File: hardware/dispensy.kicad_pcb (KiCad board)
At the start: 2 copper layers, 125 x 100 mm, 87 parts, among them SW1 BOOTSEL, SW2 RESET, U1 DBT50G-7_62-4P, U10 RP2040, U11 SS54_C22452, U12 SS54_C22452, U13 CAN_IO, U14 TJA1042T_3_1J, U15 USB-C, U16 LM2576S-5_0_TR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

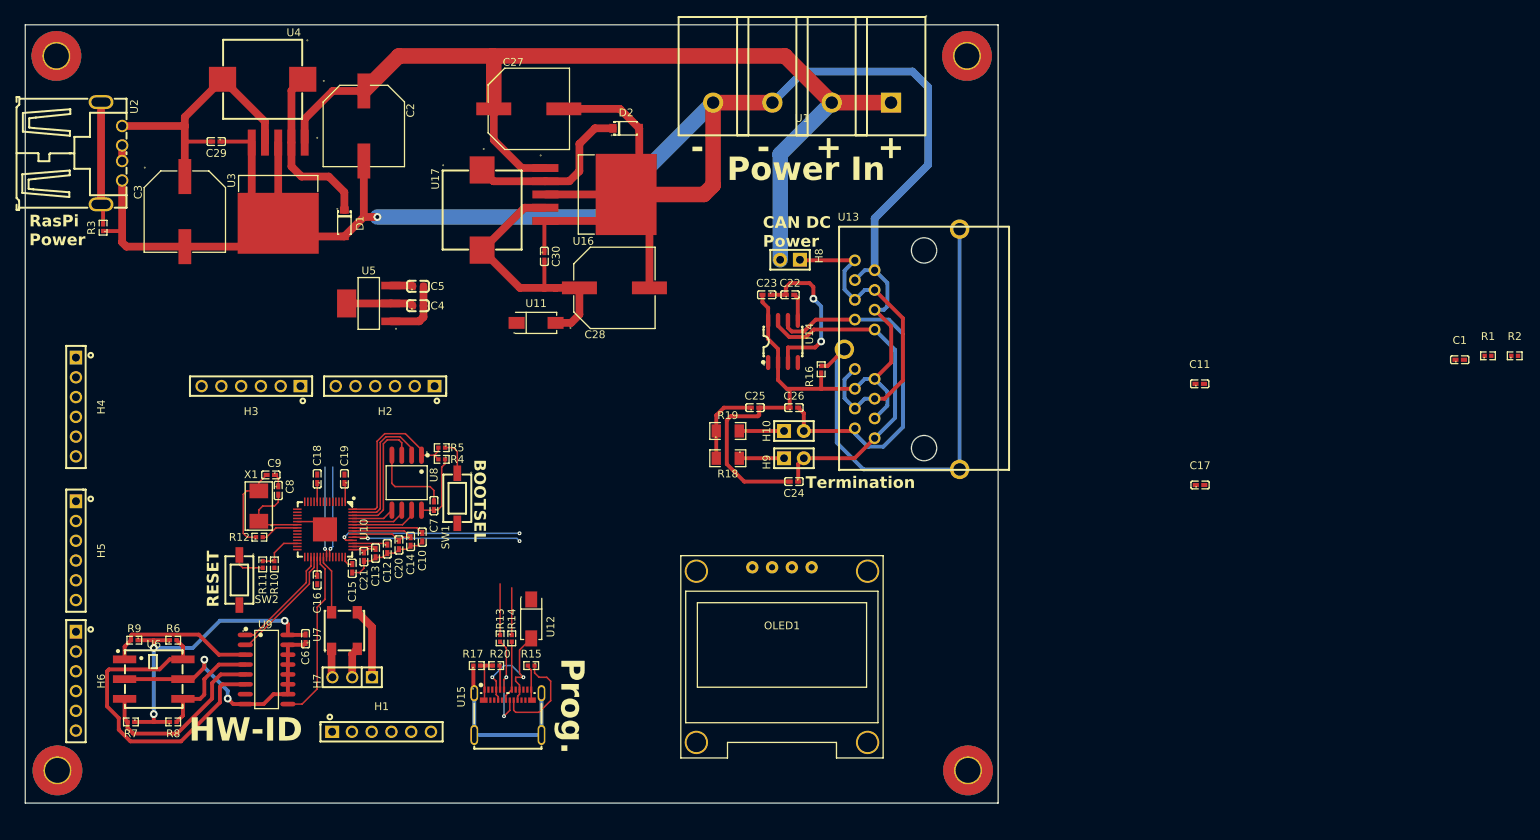
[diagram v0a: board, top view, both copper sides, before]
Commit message: more routing. all parts placed somewhere on board now.
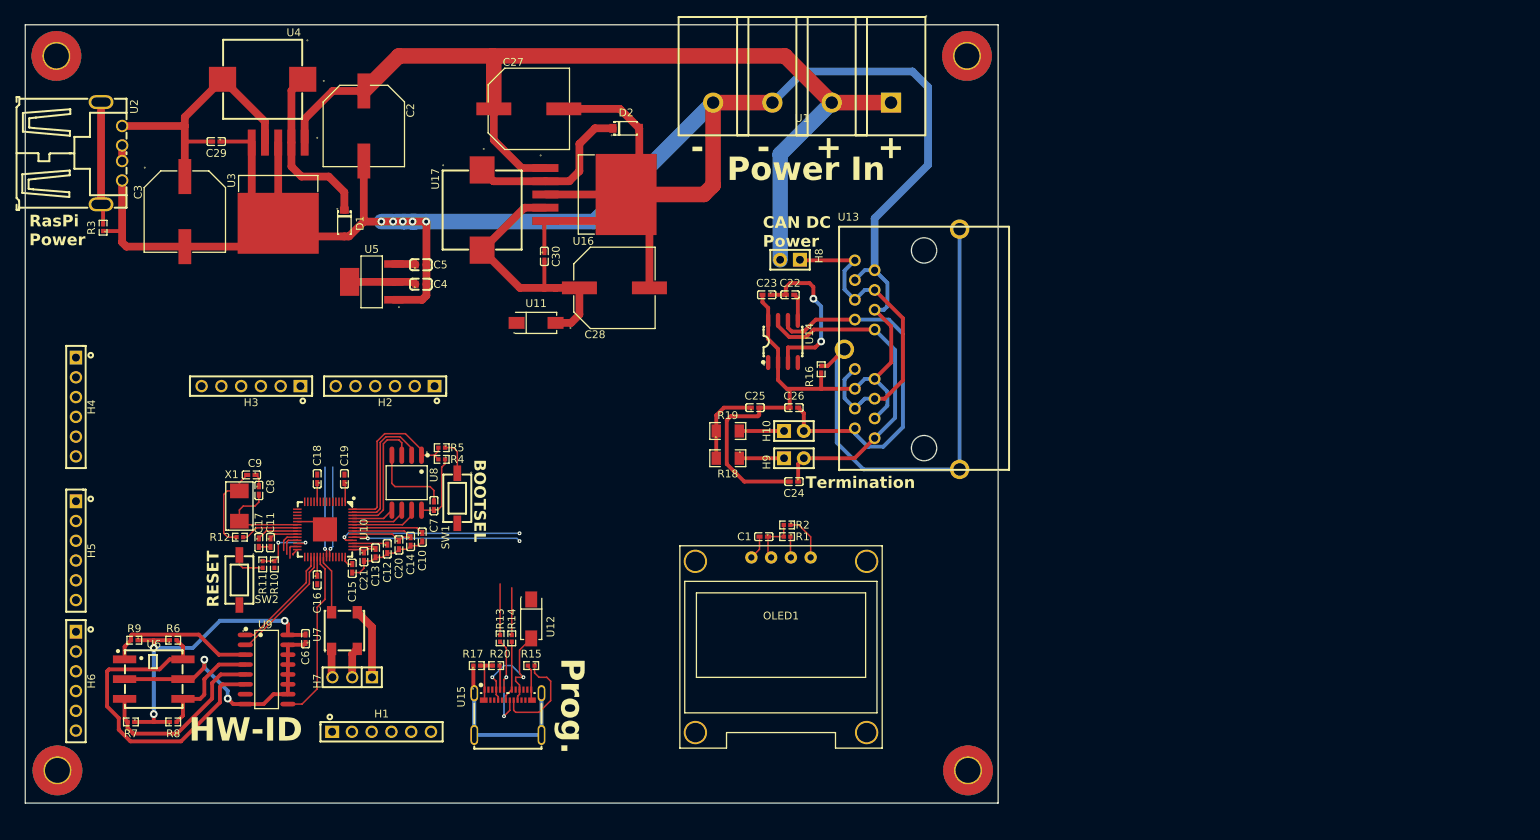
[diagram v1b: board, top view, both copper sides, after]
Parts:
- moved C17 121.2 mm to (69.0, 111.5), turned to -90 degrees
- moved C11 121.1 mm to (70.5, 111.5), turned to -90 degrees
- moved R2 96.0 mm to (136.9, 109.2), turned to 180 degrees
- moved R1 93.0 mm to (136.9, 110.7), turned to 180 degrees
- moved C1 92.3 mm to (133.9, 110.7), turned to 180 degrees
- moved C4 2.79 mm to (89.8, 78.3)
- moved C5 2.79 mm to (89.8, 75.8)
- moved U5 2.79 mm to (83.5, 78.0)
- moved C8 2.50 mm to (69.0, 104.8)
- moved C9 2.50 mm to (68.0, 102.8)
- moved R12 2.50 mm to (66.6, 110.8)
- moved X1 2.50 mm to (66.5, 106.8)
- moved OLED1 1.27 mm to (123.1, 137.9)
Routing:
- net GND: track 439.4 -> 456.4 mm, vias 3 -> 7
- net +3.3V: track 93.8 -> 105.5 mm
- net /RP2040/I2C_SDA: track 0.00 -> 5.87 mm
- net +1V1: track 13.7 -> 17.4 mm
- net /RP2040/Debug_Clock: track 0.00 -> 3.19 mm
- net /RP2040/Debug_Data: track 0.00 -> 3.03 mm
- net /RP2040/I2C_SCL: track 0.00 -> 2.70 mm
- net Net-(U10-RUN): track 6.01 -> 8.67 mm, vias 0 -> 2
- net Net-(U10-XOUT): track 4.95 -> 7.45 mm
- net Net-(U10-XIN): track 10.5 -> 13.0 mm
- net /RP2040/Debug_Tx: track 0.00 -> 2.39 mm
- net /RP2040/Debug_Rx: track 0.00 -> 0.93 mm

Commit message: add screw connector for 5v-ext
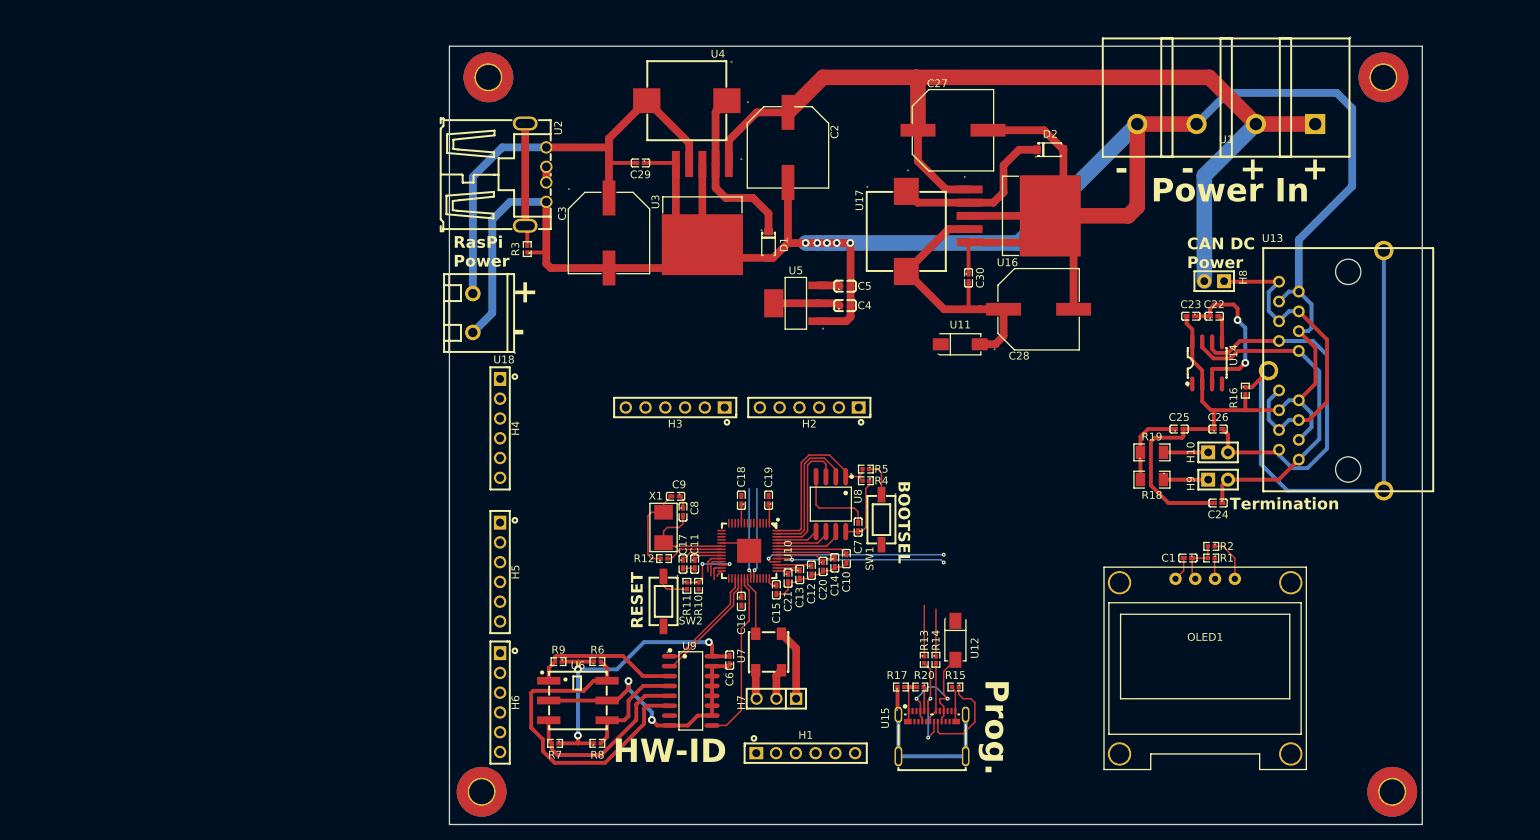
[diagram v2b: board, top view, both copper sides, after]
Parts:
- added U18: XY300V-A-5_0-2P, jlc_footprints:CONN-TH_XY300V-A-5.0-2P, F.Cu at (96.5, 82.0)
- moved H11 55.6 mm to (98.5, 51.7)
- moved R15 54.6 mm to (158.5, 130.1)
- moved R17 54.6 mm to (151.5, 130.1)
- moved R20 54.6 mm to (154.0, 130.1)
- moved U10 54.6 mm to (132.0, 112.6)
- moved U11 54.6 mm to (159.1, 86.0)
- moved U9 54.6 mm to (124.5, 130.6)
- moved C1 54.6 mm to (188.4, 113.5)
- moved C10 54.6 mm to (144.5, 113.6)
- moved C11 54.6 mm to (125.0, 114.2)
- moved C12 54.6 mm to (140.0, 115.1)
- moved C13 54.6 mm to (138.5, 115.6)
- moved C14 54.6 mm to (143.0, 114.1)
- moved C15 54.6 mm to (135.5, 117.6)
- moved C16 54.6 mm to (131.0, 119.1)
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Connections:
- net /External PSU/Vout renamed /EXT_PSU/Vout
- net /RP2040/5V PSU/Vout renamed /PI/PI_PSU/Vout
- net /RP2040/ADC0 renamed /PI/ADC0
- net /RP2040/ADC1 renamed /PI/ADC1
- net /RP2040/ADC2 renamed /PI/ADC2
- net /RP2040/ADC3 renamed /PI/ADC3
- net /RP2040/Debug_Clock renamed /PI/Debug_Clock
- net /RP2040/Debug_Data renamed /PI/Debug_Data
- net /RP2040/Debug_Rx renamed /PI/Debug_Rx
- net /RP2040/Debug_Tx renamed /PI/Debug_Tx
- net /RP2040/I2C_SCL renamed /PI/I2C_SCL
- net /RP2040/I2C_SDA renamed /PI/I2C_SDA
- net /RP2040/IO0 renamed /PI/IO0
- net /RP2040/IO1 renamed /PI/IO1
- net /RP2040/IO10 renamed /PI/IO10
- net /RP2040/IO11 renamed /PI/IO11
- net /RP2040/IO12 renamed /PI/IO12
- net /RP2040/IO13 renamed /PI/IO13
- net /RP2040/IO14 renamed /PI/IO14
- net /RP2040/IO15 renamed /PI/IO15
- net /RP2040/IO2 renamed /PI/IO2
- net /RP2040/IO3 renamed /PI/IO3
- net /RP2040/IO4 renamed /PI/IO4
- net /RP2040/IO5 renamed /PI/IO5
- net /RP2040/IO6 renamed /PI/IO6
- net /RP2040/IO7 renamed /PI/IO7
- net /RP2040/IO8 renamed /PI/IO8
- net /RP2040/IO9 renamed /PI/IO9
- net /RP2040/LED_Din renamed /PI/LED_Din
- net /RP2040/SPI_FLASH.SCLK renamed /PI/SPI_FLASH.SCLK
- net /RP2040/SPI_FLASH.SD0 renamed /PI/SPI_FLASH.SD0
- net /RP2040/SPI_FLASH.SD1 renamed /PI/SPI_FLASH.SD1
- net /RP2040/SPI_FLASH.SD2 renamed /PI/SPI_FLASH.SD2
- net /RP2040/SPI_FLASH.SD3 renamed /PI/SPI_FLASH.SD3
- net /RP2040/SPI_FLASH.SS renamed /PI/SPI_FLASH.SS
- net /RP2040/SR_Clock renamed /PI/SR_Clock
- net /RP2040/SR_Data renamed /PI/SR_Data
- net /RP2040/SR_Load renamed /PI/SR_Load
- net /RP2040/USBC.DM renamed /PI/USBC.DM
- net /RP2040/USBC.DP renamed /PI/USBC.DP
- net /RP2040/USBC.SHIELD renamed /PI/USBC.SHIELD
- net /RP2040/USBC.VBUS renamed /PI/USBC.VBUS
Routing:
- net /EXT_PSU/Vout: track 36.5 -> 62.5 mm
- net GND: track 456.4 -> 479.8 mm
